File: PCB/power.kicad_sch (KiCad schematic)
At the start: 13 parts, among them J1 USB_C_Receptacle_USB2.0_16P, J2 BAT, U2 MCP73833-xxx-UN

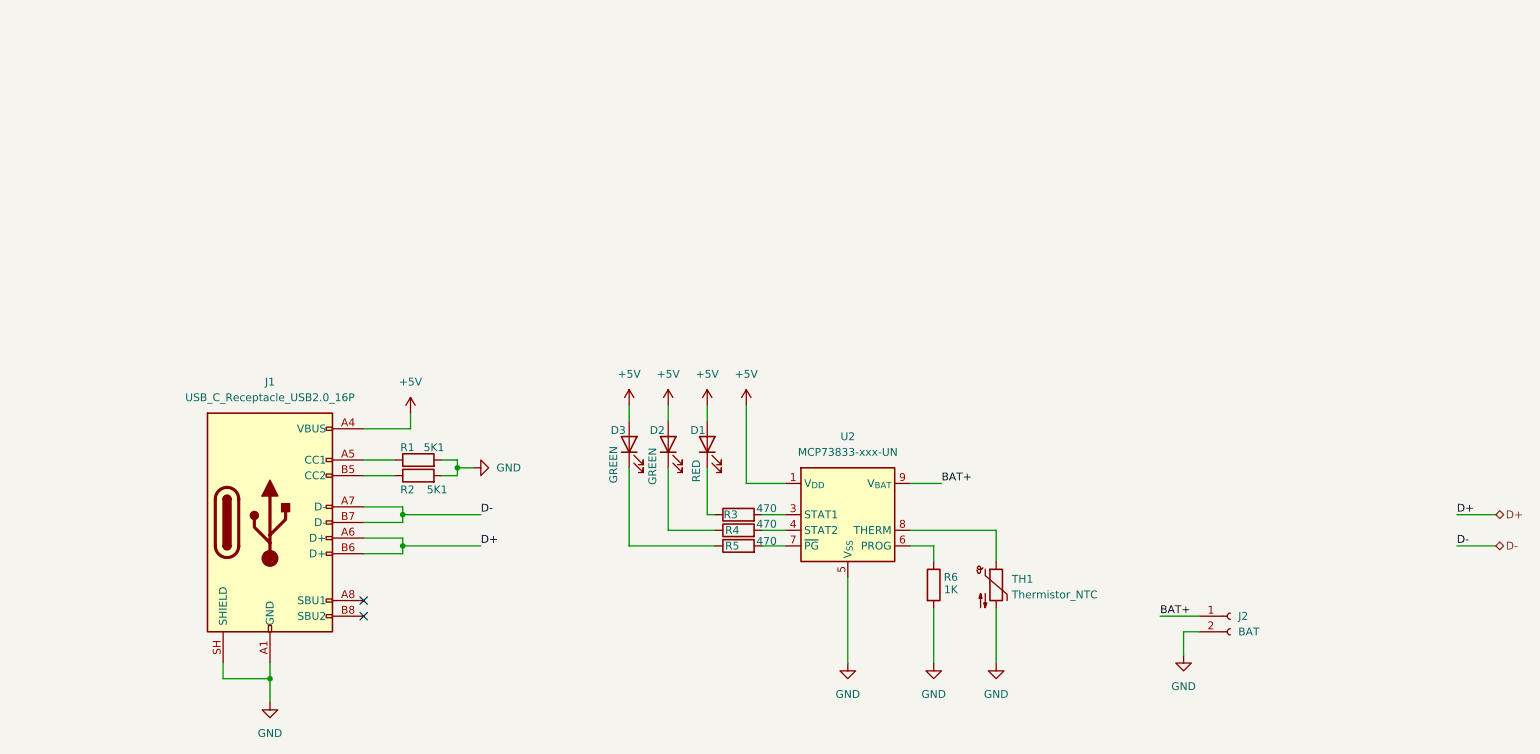
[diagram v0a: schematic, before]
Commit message: RFID sch added
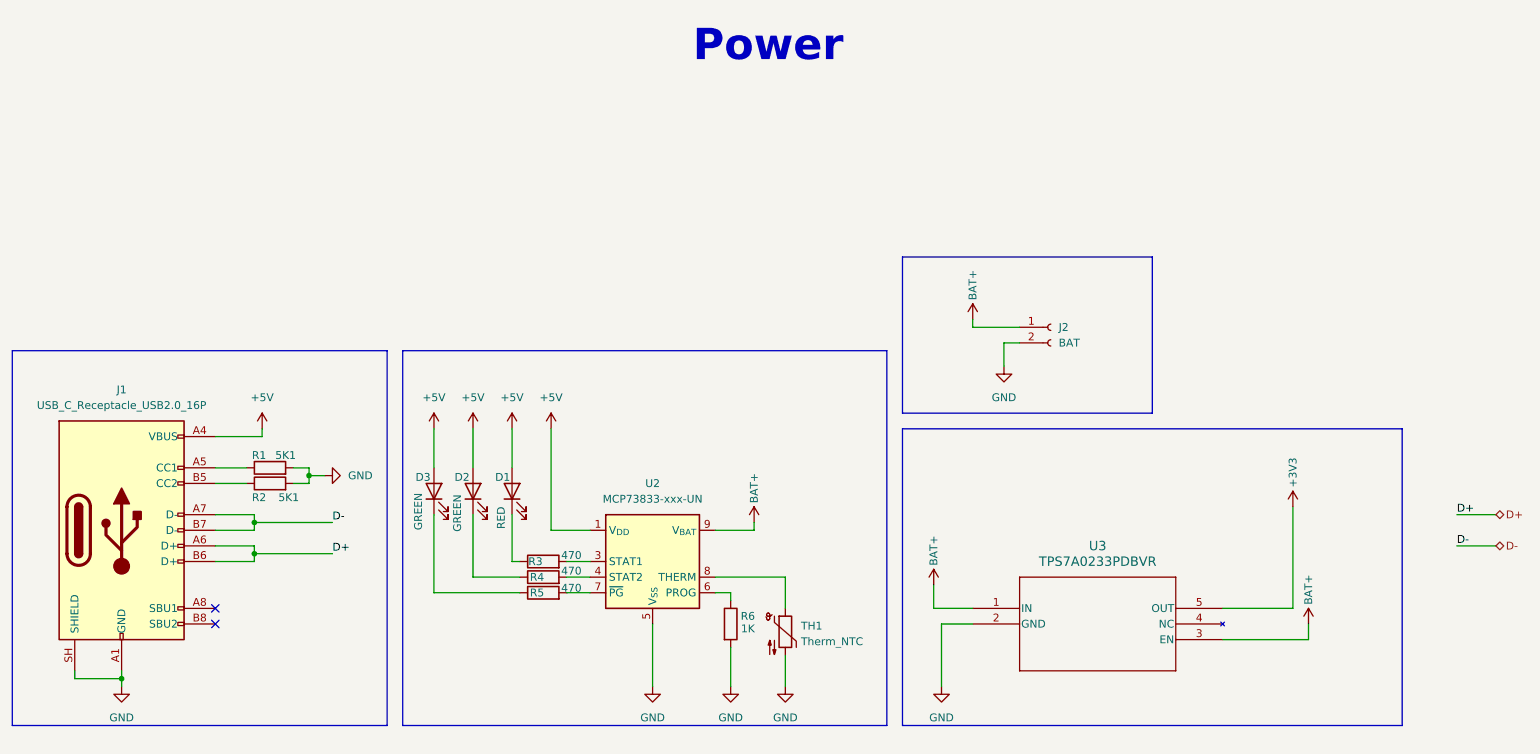
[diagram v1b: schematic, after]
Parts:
- added U3: TPS7A0233PDBVR, External:SOT23_DBV_TEX-L, symbol External:TPS7A0233PDBVR
- TH1: value Thermistor_NTC -> Therm_NTC
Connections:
- net BAT+: now also U3.1 (IN), U3.3 (EN)
- net GND: now also U3.2 (GND)
- new net +3V3: U3.5 (OUT)
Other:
- note added: "Power"
- moved on the sheet: D1, D2, D3, J1, J2, R1, R2, R3, R4, R5, R6, TH1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
